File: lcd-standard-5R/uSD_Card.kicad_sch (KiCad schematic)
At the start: 7 parts, among them J4 Micro_SD_Card_Det1

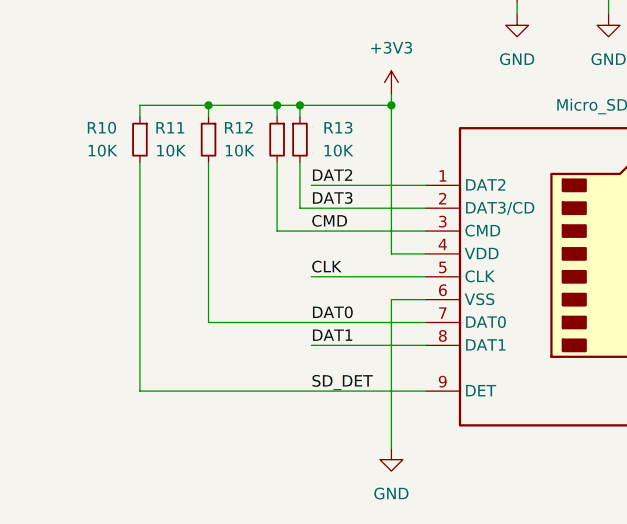
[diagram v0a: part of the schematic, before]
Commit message: Change MCU to STM32H743
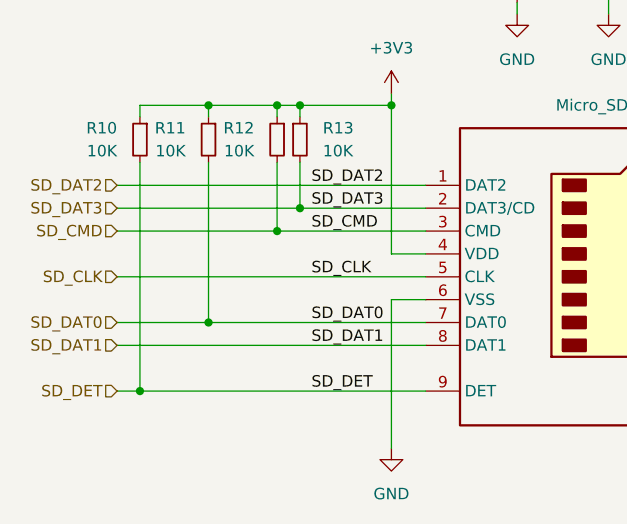
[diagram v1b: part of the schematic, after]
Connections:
- net CLK renamed SD_CLK
- net CMD renamed SD_CMD
- net DAT0 renamed SD_DAT0
- net DAT1 renamed SD_DAT1
- net DAT2 renamed SD_DAT2
- net DAT3 renamed SD_DAT3
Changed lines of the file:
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@@
+	)
+	(junction
+		(at 102.87 110.49)
+		(diameter 0)
+		(color 0 0 0 0)
 	)
 	(junction
@@
 		(color 0 0 0 0)
 	)
+	(junction
+		(at 110.49 102.87)
+		(diameter 0)
+		(color 0 0 0 0)
+	)
+	(junction
+		(at 118.11 92.71)
+		(diameter 0)
+		(color 0 0 0 0)
+	)
+	(junction
+		(at 120.65 90.17)
+		(diameter 0)
+		(color 0 0 0 0)
+	)
+	(wire
+		(pts
+			(xy 100.33 97.79) (xy 134.62 97.79)
+		)
+		(stroke
+			(width 0)
+			(type default)
+		)
+	)
 	(wire
 		(pts
@@
 	(wire
 		(pts
-			(xy 121.92 97.79) (xy 134.62 97.79)
-		)
-		(stroke
-			(width 0)
-			(type default)
-		)
-	)
-	(wire
-		(pts
 			(xy 102.87 80.01) (xy 102.87 78.74)
 		)
@@
 	(wire
 		(pts
-			(xy 121.92 105.41) (xy 134.62 105.41)
+			(xy 100.33 92.71) (xy 118.11 92.71)
 		)
 		(stroke
@@
 	(wire
 		(pts
-			(xy 121.92 87.63) (xy 134.62 87.63)
-		)
-		(stroke
-			(width 0)
-			(type default)
-		)
-	)
-	(wire
-		(pts
 			(xy 118.11 78.74) (xy 118.11 80.01)
 		)
@@
 	(wire
 		(pts
+			(xy 100.33 105.41) (xy 134.62 105.41)
+		)
+		(stroke
+			(width 0)
+			(type default)
+		)
+	)
+	(wire
+		(pts
+			(xy 100.33 110.49) (xy 102.87 110.49)
+		)
+		(stroke
+			(width 0)
+			(type default)
+		)
+	)
+	(wire
+		(pts
 			(xy 179.07 110.49) (xy 179.07 116.84)
 		)
@@
 	(wire
 		(pts
+			(xy 100.33 102.87) (xy 110.49 102.87)
+		)
+		(stroke
+			(width 0)
+			(type default)
+		)
+	)
+	(wire
+		(pts
 			(xy 118.11 85.09) (xy 118.11 92.71)
 		)
@@
 	(wire
 		(pts
+			(xy 100.33 90.17) (xy 120.65 90.17)
+		)
+		(stroke
+			(width 0)
+			(type default)
+		)
+	)
+	(wire
+		(pts
 			(xy 144.78 58.42) (xy 144.78 59.69)
 		)
@@
 	(wire
 		(pts
+			(xy 100.33 87.63) (xy 134.62 87.63)
+		)
+		(stroke
+			(width 0)
+			(type default)
+		)
+	)
+	(wire
+		(pts
 			(xy 130.81 78.74) (xy 130.81 95.25)
 		)
@@
 		)
 	)
-	(label "DAT2"
+	(label "SD_DAT0"
+		(at 121.92 102.87 0)
+		(fields_autoplaced yes)
+		(effects
+			(font
+				(size 1.27 1.27)
+			)
+			(justify left bottom)
+		)
+	)
+	(label "SD_DAT1"
+		(at 121.92 105.41 0)
+		(fields_autoplaced yes)
+		(effects
+			(font
+				(size 1.27 1.27)
+			)
+			(justify left bottom)
+		)
+	)
+	(label "SD_CLK"
+		(at 121.92 97.79 0)
+		(fields_autoplaced yes)
+		(effects
+			(font
+				(size 1.27 1.27)
+			)
+			(justify left bottom)
+		)
+	)
+	(label "SD_CMD"
+		(at 121.92 92.71 0)
+		(fields_autoplaced yes)
+		(effects
+			(font
+				(size 1.27 1.27)
+			)
+			(justify left bottom)
+		)
+	)
+	(label "SD_DAT2"
 		(at 121.92 87.63 0)
-		(fields_autoplaced yes)
-		(effects
-			(font
-				(size 1.27 1.27)
-			)
-			(justify left bottom)
-		)
-	)
-	(label "DAT3"
-		(at 121.92 90.17 0)
-		(fields_autoplaced yes)
-		(effects
-			(font
-				(size 1.27 1.27)
-			)
-			(justify left bottom)
-		)
-	)
-	(label "DAT0"
-		(at 121.92 102.87 0)
-		(fields_autoplaced yes)
-		(effects
-			(font
-				(size 1.27 1.27)
-			)
-			(justify left bottom)
-		)
-	)
-	(label "DAT1"
-		(at 121.92 105.41 0)
-		(fields_autoplaced yes)
-		(effects
-			(font
-				(size 1.27 1.27)
-			)
-			(justify left bottom)
-		)
-	)
-	(label "CLK"
-		(at 121.92 97.79 0)
 		(fields_autoplaced yes)
 		(effects
@@
 		)
 	)
-	(label "CMD"
-		(at 121.92 92.71 0)
-		(fields_autoplaced yes)
-		(effects
-			(font
-				(size 1.27 1.27)
-			)
-			(justify left bottom)
-		)
-	)
+	(label "SD_DAT3"
+		(at 121.92 90.17 0)
+		(fields_autoplaced yes)
+		(effects
+			(font
+				(size 1.27 1.27)
+			)
+			(justify left bottom)
+		)
+	)
+	(hierarchical_label "SD_DET"
+		(shape input)
+		(at 100.33 110.49 180)
+		(fields_autoplaced yes)
+		(effects
+			(font
+				(size 1.27 1.27)
+			)
+			(justify right)
+		)
+	)
+	(hierarchical_label "SD_DAT0"
+		(shape input)
+		(at 100.33 102.87 180)
+		(fields_autoplaced yes)
+		(effects
+			(font
+				(size 1.27 1.27)
+			)
+			(justify right)
+		)
+	)
+	(hierarchical_label "SD_CLK"
+		(shape input)
+		(at 100.33 97.79 180)
+		(fields_autoplaced yes)
+		(effects
+			(font
+				(size 1.27 1.27)
+			)
+			(justify right)
+		)
+	)
+	(hierarchical_label "SD_DAT1"
+		(shape input)
+		(at 100.33 105.41 180)
+		(fields_autoplaced yes)
+		(effects
+			(font
+				(size 1.27 1.27)
+			)
+			(justify right)
+		)
+	)
+	(hierarchical_label "SD_CMD"
+		(shape input)
+		(at 100.33 92.71 180)
+		(fields_autoplaced yes)
+		(effects
+			(font
+				(size 1.27 1.27)
+			)
+			(justify right)
+		)
+	)
+	(hierarchical_label "SD_DAT3"
+		(shape input)
+		(at 100.33 90.17 180)
+		(fields_autoplaced yes)
+		(effects
+			(font
+				(size 1.27 1.27)
+			)
+			(justify right)
+		)
+	)
+	(hierarchical_label "SD_DAT2"
+		(shape input)
+		(at 100.33 87.63 180)
+		(fields_autoplaced yes)
+		(effects
+			(font
+				(size 1.27 1.27)
+			)
+			(justify right)
+		)
+	)

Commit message: Change 10P CTP to omron type
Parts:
- C39: JLCPCB Part # C1525 -> C307331
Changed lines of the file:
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@@
 			)
 		)
-		(property "JLCPCB Part #" "C1525"
+		(property "JLCPCB Part #" "C307331"
 			(at 154.94 63.5 0)
 			(effects

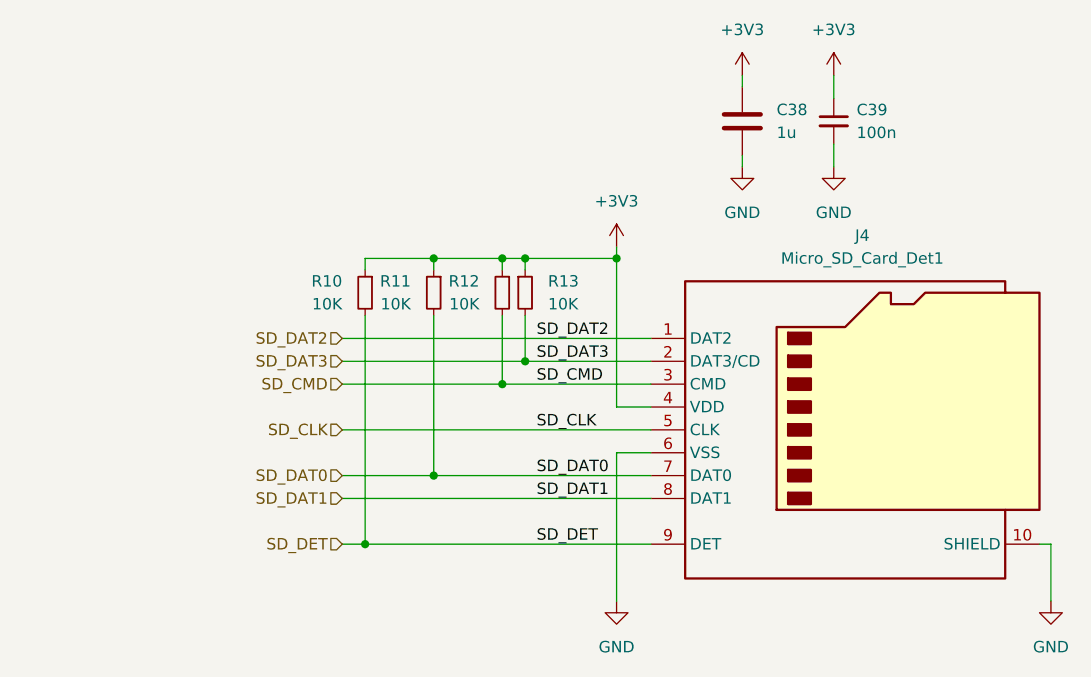
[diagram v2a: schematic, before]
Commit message: Finished SDRAM, LCD (need checkup with CubeIDE), RTP touch controll
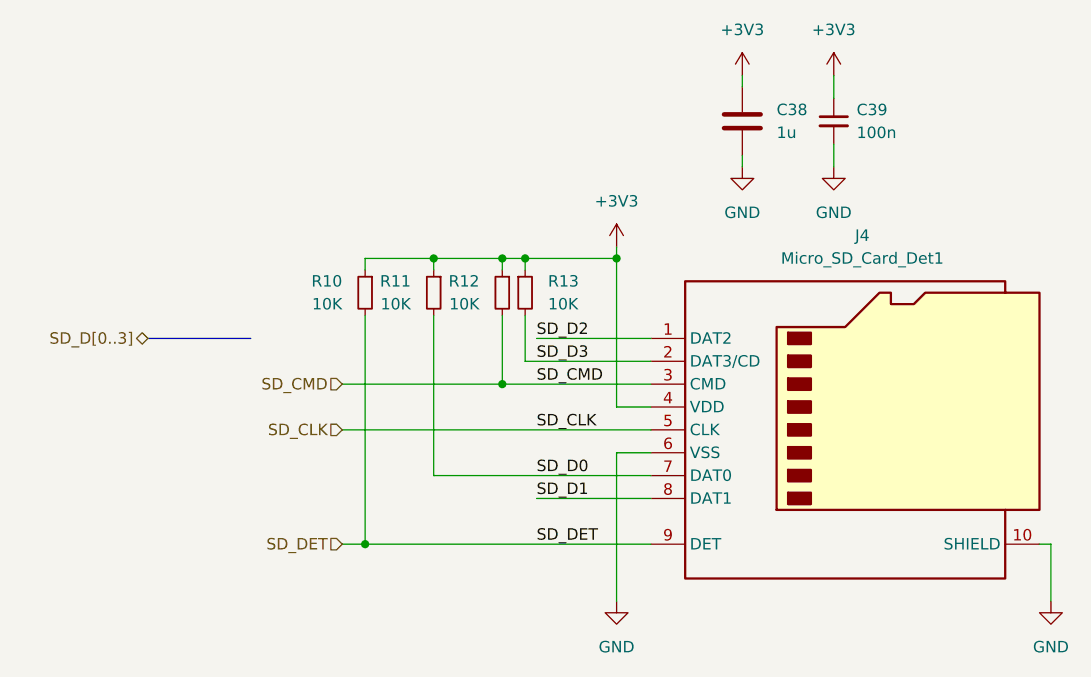
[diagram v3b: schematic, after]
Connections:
- net SD_DAT0 renamed SD_D0
- net SD_DAT1 renamed SD_D1
- net SD_DAT2 renamed SD_D2
- net SD_DAT3 renamed SD_D3
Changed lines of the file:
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@@
-	)
-	(junction
-		(at 110.49 102.87)
-		(diameter 0)
-		(color 0 0 0 0)
 	)
 	(junction
@@
 		(color 0 0 0 0)
 	)
-	(junction
-		(at 120.65 90.17)
-		(diameter 0)
-		(color 0 0 0 0)
-	)
 	(wire
 		(pts
@@
 	(wire
 		(pts
+			(xy 121.92 87.63) (xy 134.62 87.63)
+		)
+		(stroke
+			(width 0)
+			(type default)
+		)
+	)
+	(wire
+		(pts
 			(xy 102.87 110.49) (xy 134.62 110.49)
 		)
@@
 	(wire
 		(pts
+			(xy 121.92 105.41) (xy 134.62 105.41)
+		)
+		(stroke
+			(width 0)
+			(type default)
+		)
+	)
+	(wire
+		(pts
 			(xy 130.81 77.47) (xy 130.81 78.74)
 		)
@@
 	(wire
 		(pts
-			(xy 100.33 105.41) (xy 134.62 105.41)
-		)
-		(stroke
-			(width 0)
-			(type default)
-		)
-	)
-	(wire
-		(pts
 			(xy 100.33 110.49) (xy 102.87 110.49)
 		)
@@
 	(wire
 		(pts
-			(xy 100.33 102.87) (xy 110.49 102.87)
-		)
-		(stroke
-			(width 0)
-			(type default)
-		)
-	)
-	(wire
-		(pts
 			(xy 118.11 85.09) (xy 118.11 92.71)
 		)
@@
 		)
 	)
+	(bus
+		(pts
+			(xy 78.74 87.63) (xy 90.17 87.63)
+		)
+		(stroke
+			(width 0)
+			(type default)
+		)
+	)
 	(wire
 		(pts
@@
 	(wire
 		(pts
-			(xy 100.33 90.17) (xy 120.65 90.17)
-		)
-		(stroke
-			(width 0)
-			(type default)
-		)
-	)
-	(wire
-		(pts
 			(xy 144.78 58.42) (xy 144.78 59.69)
 		)
@@
 	(wire
 		(pts
-			(xy 100.33 87.63) (xy 134.62 87.63)
-		)
-		(stroke
-			(width 0)
-			(type default)
-		)
-	)
-	(wire
-		(pts
 			(xy 130.81 78.74) (xy 130.81 95.25)
 		)
@@
 		)
 	)
-	(label "SD_DAT0"
-		(at 121.92 102.87 0)
-		(fields_autoplaced yes)
-		(effects
-			(font
-				(size 1.27 1.27)
-			)
-			(justify left bottom)
-		)
-	)
-	(label "SD_DAT1"
-		(at 121.92 105.41 0)
+	(label "SD_D2"
+		(at 121.92 87.63 0)
+		(fields_autoplaced yes)
+		(effects
+			(font
+				(size 1.27 1.27)
+			)
+			(justify left bottom)
+		)
+	)
+	(label "SD_D3"
+		(at 121.92 90.17 0)
 		(fields_autoplaced yes)
 		(effects
@@
 		)
 	)
-	(label "SD_DAT2"
-		(at 121.92 87.63 0)
+	(label "SD_D0"
+		(at 121.92 102.87 0)
+		(fields_autoplaced yes)
+		(effects
+			(font
+				(size 1.27 1.27)
+			)
+			(justify left bottom)
+		)
+	)
+	(label "SD_D1"
+		(at 121.92 105.41 0)
 		(fields_autoplaced yes)
 		(effects
@@
 	(label "SD_DET"
 		(at 121.92 110.49 0)
-		(fields_autoplaced yes)
-		(effects
-			(font
-				(size 1.27 1.27)
-			)
-			(justify left bottom)
-		)
-	)
-	(label "SD_DAT3"
-		(at 121.92 90.17 0)
 		(fields_autoplaced yes)
 		(effects
@@
 		)
 	)
-	(hierarchical_label "SD_DAT0"
-		(shape input)
-		(at 100.33 102.87 180)
+	(hierarchical_label "SD_D[0..3]"
+		(shape bidirectional)
+		(at 78.74 87.63 180)
 		(fields_autoplaced yes)
 		(effects
@@
 		)
 	)
-	(hierarchical_label "SD_DAT1"
-		(shape input)
-		(at 100.33 105.41 180)
-		(fields_autoplaced yes)
-		(effects
-			(font
-				(size 1.27 1.27)
-			)
-			(justify right)
-		)
-	)
 	(hierarchical_label "SD_CMD"
 		(shape input)
@@
 		(fields_autoplaced yes)
 		(effects
-			(font
-				(size 1.27 1.27)
-			)
-			(justify right)
-		)
-	)
-	(hierarchical_label "SD_DAT3"
-		(shape input)
-		(at 100.33 90.17 180)
-		(fields_autoplaced yes)
-		(effects
-			(font
-				(size 1.27 1.27)
-			)
-			(justify right)
-		)
-	)
-	(hierarchical_label "SD_DAT2"
-		(shape input)
-		(at 100.33 87.63 180)
-		(fields_autoplaced yes)
-		(effects
